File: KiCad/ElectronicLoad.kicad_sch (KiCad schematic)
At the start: 180 parts, among them J1 LOAD, J2 SMA2, J3 SMA1, J4 12V, J5 USB, J6 PROG, M1 FAN, Q1 any, Q2 any, Q3 BSS138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

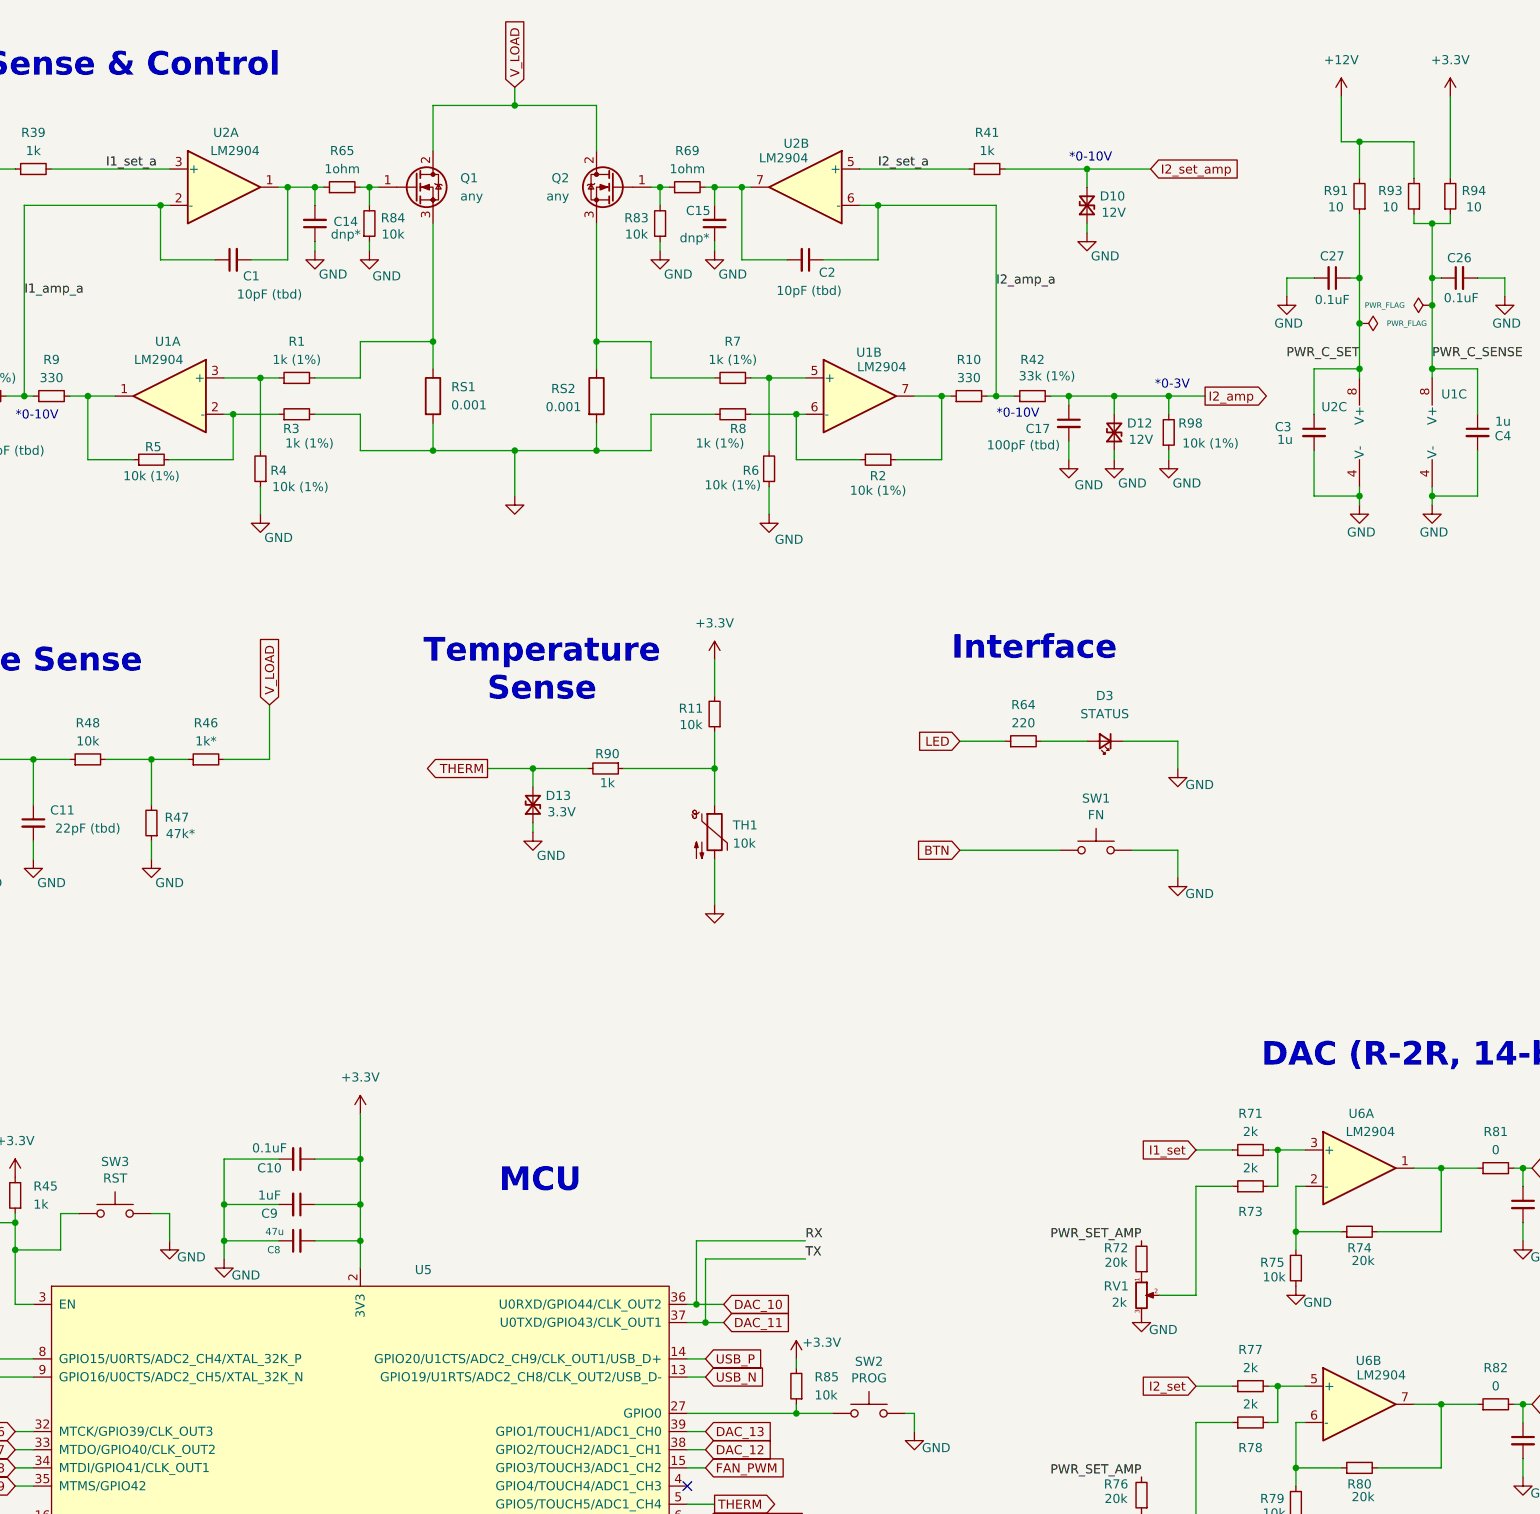
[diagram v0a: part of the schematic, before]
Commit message: ESP32-S2 support + improved firmware
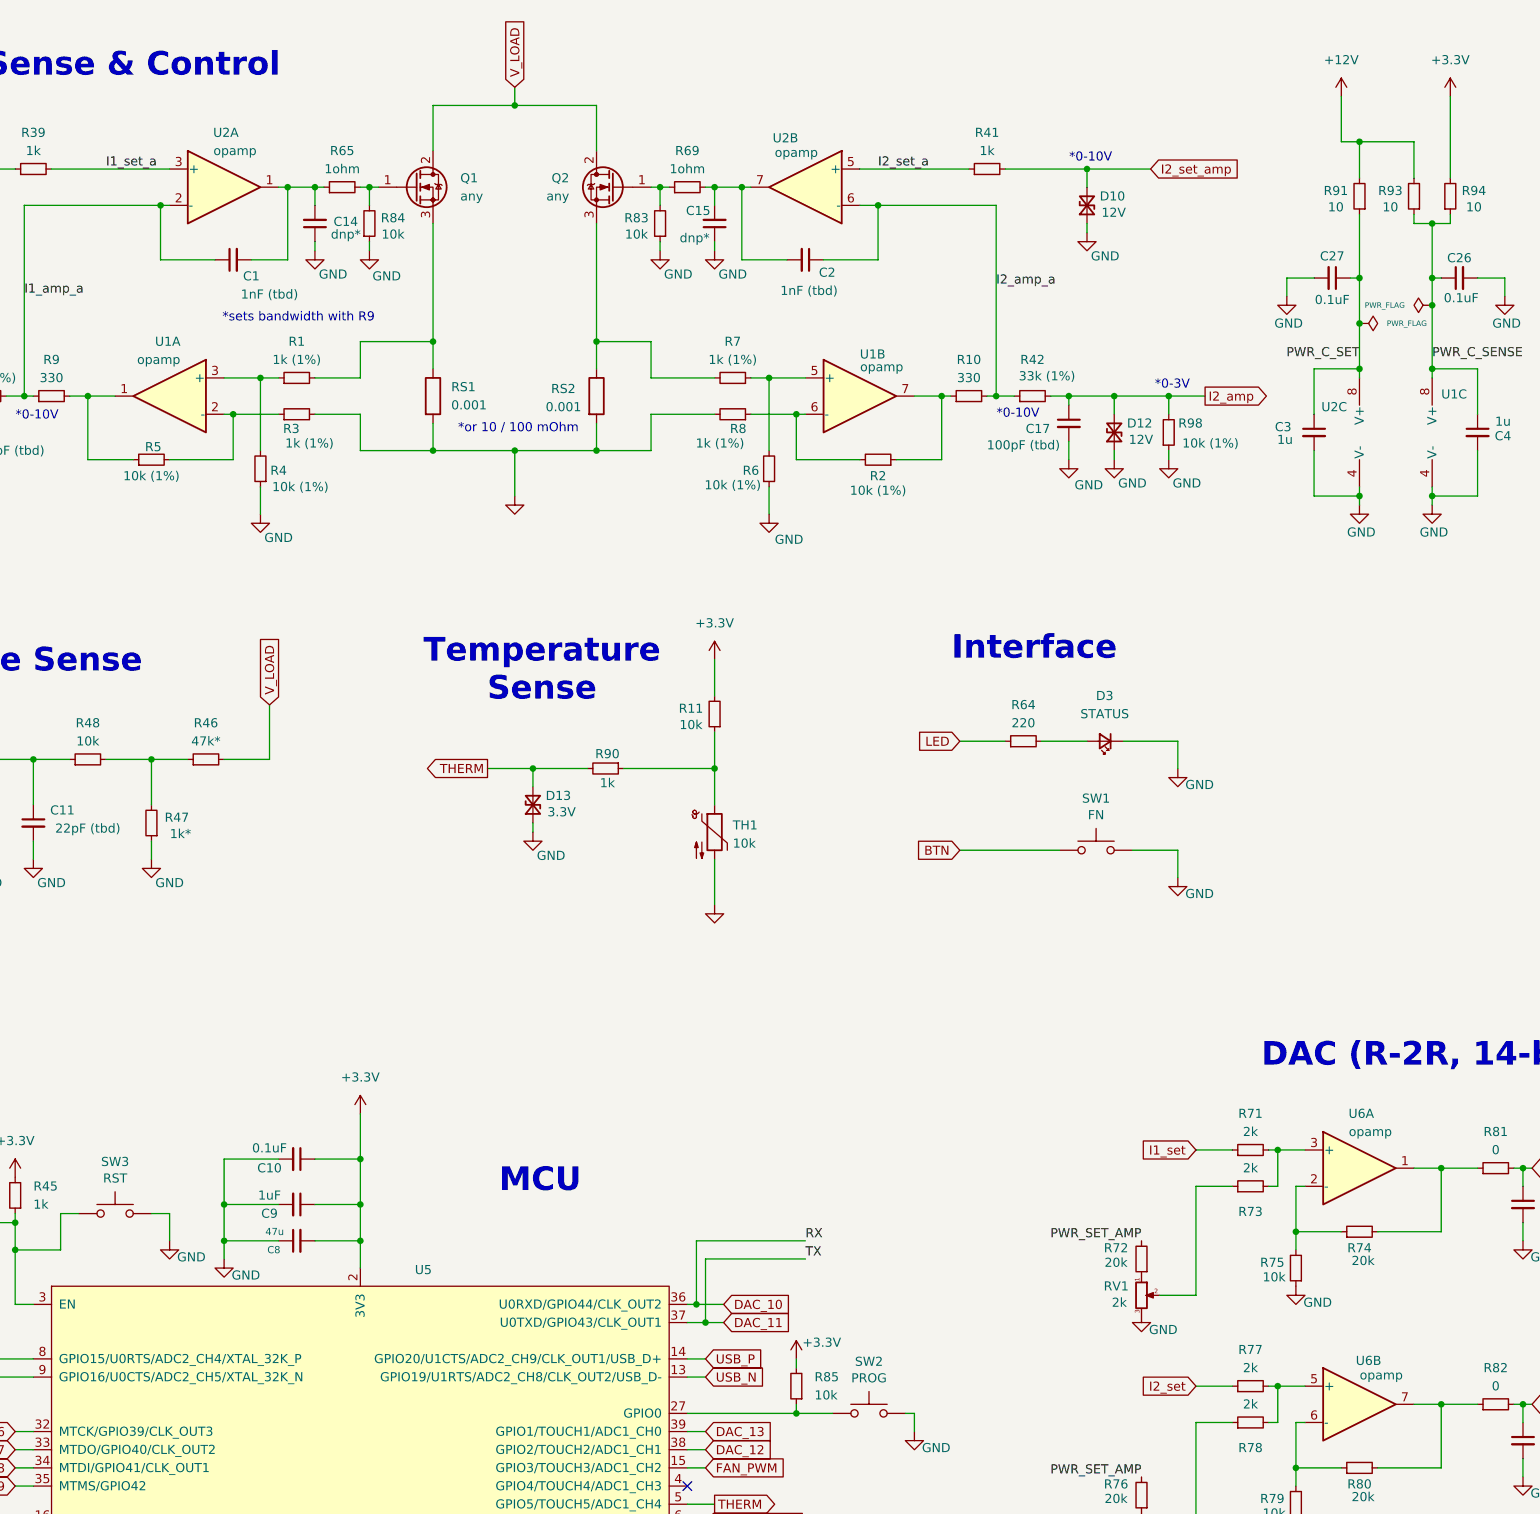
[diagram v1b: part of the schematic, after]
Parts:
- C1, C2: value 10pF (tbd) -> 1nF (tbd)
- R46: value 1k* -> 47k*
- R47: value 47k* -> 1k*
- U1, U2, U6: value LM2904 -> opamp
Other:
- note added: "*or 10 / 100 mOhm"
- note added: "*sets bandwidth with R9"
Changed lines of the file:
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@@
 		)
 	)
+	(text "*or 10 / 100 mOhm"
+		(exclude_from_sim no)
+		(at 122.428 71.882 0)
+		(effects
+			(font
+				(size 1.27 1.27)
+			)
+		)
+	)
+	(text "*sets bandwidth with R9"
+		(exclude_from_sim no)
+		(at 91.694 56.388 0)
+		(effects
+			(font
+				(size 1.27 1.27)
+			)
+		)
+	)
 	(text "*0-10V"
 		(exclude_from_sim no)
@@
 			)
 		)
-		(property "Value" "LM2904"
+		(property "Value" "opamp"
 			(at 72.136 62.23 0)
 			(effects
@@
 			)
 		)
-		(property "Value" "47k*"
+		(property "Value" "1k*"
 			(at 75.184 128.524 0)
 			(effects
@@
 			)
 		)
-		(property "Value" "LM2904"
+		(property "Value" "opamp"
 			(at 82.804 33.02 0)
 			(effects
@@
 			)
 		)
-		(property "Value" "10pF (tbd)"
+		(property "Value" "1nF (tbd)"
 			(at 87.63 53.086 90)
 			(effects
@@
 		(dnp no)
 		(property "Reference" "U1"
-			(at 171.45 61.214 0)
+			(at 171.958 61.468 0)
 			(effects
 				(font
@@
 			)
 		)
-		(property "Value" "LM2904"
+		(property "Value" "opamp"
 			(at 173.228 63.246 0)
 			(effects
@@
 			)
 		)
-		(property "Value" "LM2904"
+		(property "Value" "opamp"
 			(at 279.908 201.422 0)
 			(effects
@@
 			)
 		)
-		(property "Value" "LM2904"
+		(property "Value" "opamp"
 			(at 241.554 77.47 0)
 			(effects
@@
 			)
 		)
-		(property "Value" "LM2904"
+		(property "Value" "opamp"
 			(at 243.078 204.216 0)
 			(effects
@@
 			)
 		)
-		(property "Value" "LM2904"
+		(property "Value" "opamp"
 			(at 241.808 68.072 0)
 			(effects
@@
 			)
 		)
-		(property "Value" "10pF (tbd)"
+		(property "Value" "1nF (tbd)"
 			(at 163.068 52.578 90)
 			(effects
@@
 			)
 		)
-		(property "Value" "LM2904"
+		(property "Value" "opamp"
 			(at 241.554 170.18 0)
 			(effects
@@
 		(on_board yes)
 		(dnp no)
-		(fields_autoplaced yes)
 		(property "Reference" "RS1"
 			(at 113.03 66.0399 0)
@@
 			)
 		)
-		(property "Value" "1k*"
+		(property "Value" "47k*"
 			(at 78.74 115.57 90)
 			(effects
@@
 		(dnp no)
 		(property "Reference" "U2"
-			(at 161.29 32.004 0)
+			(at 159.766 31.242 0)
 			(effects
 				(font
@@
 			)
 		)
-		(property "Value" "LM2904"
-			(at 159.512 34.036 0)
+		(property "Value" "opamp"
+			(at 161.29 33.274 0)
 			(effects
 				(font
